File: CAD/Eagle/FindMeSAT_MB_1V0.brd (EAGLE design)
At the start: 99 x 49.2 mm, 115 parts, among them IC1111 LM2831YMF, J291 MCX-J-P-X-RA-SM1, J701 MOLEX_105017-0001, J801 MICROSIM-8P_SDCARD-8P_MOLEX-1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, J901 JST_S3B-XH-A, Q101 ABS07, U1001 CFPT-141, U101 ATXMEGA256A3BU-AU, U1011 OPA354, U1021 OPA354, U1121 LM4120IM5-3.0, U201 SIM808, U301 MPU-9250, U401 BMP180, U501 SHT31-DIS

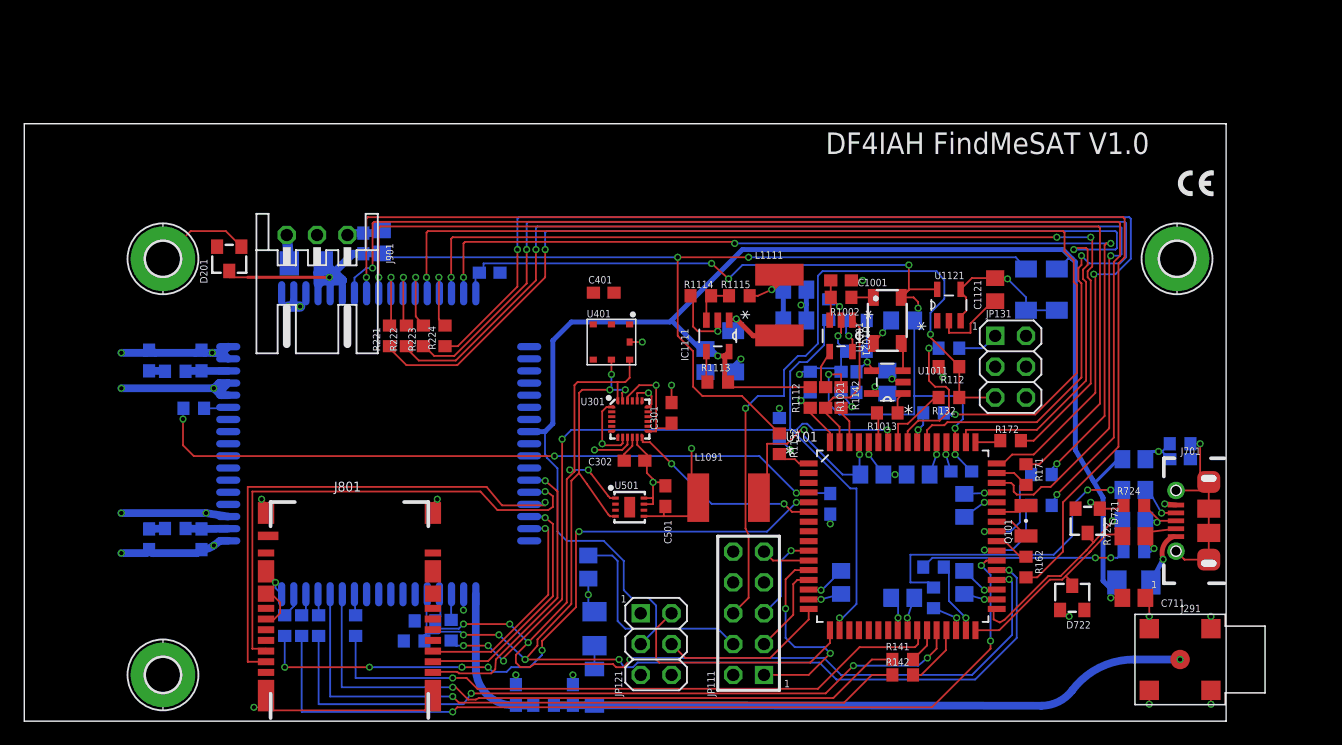
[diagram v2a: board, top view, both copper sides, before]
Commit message: Eagle - AX5243 included and library works done
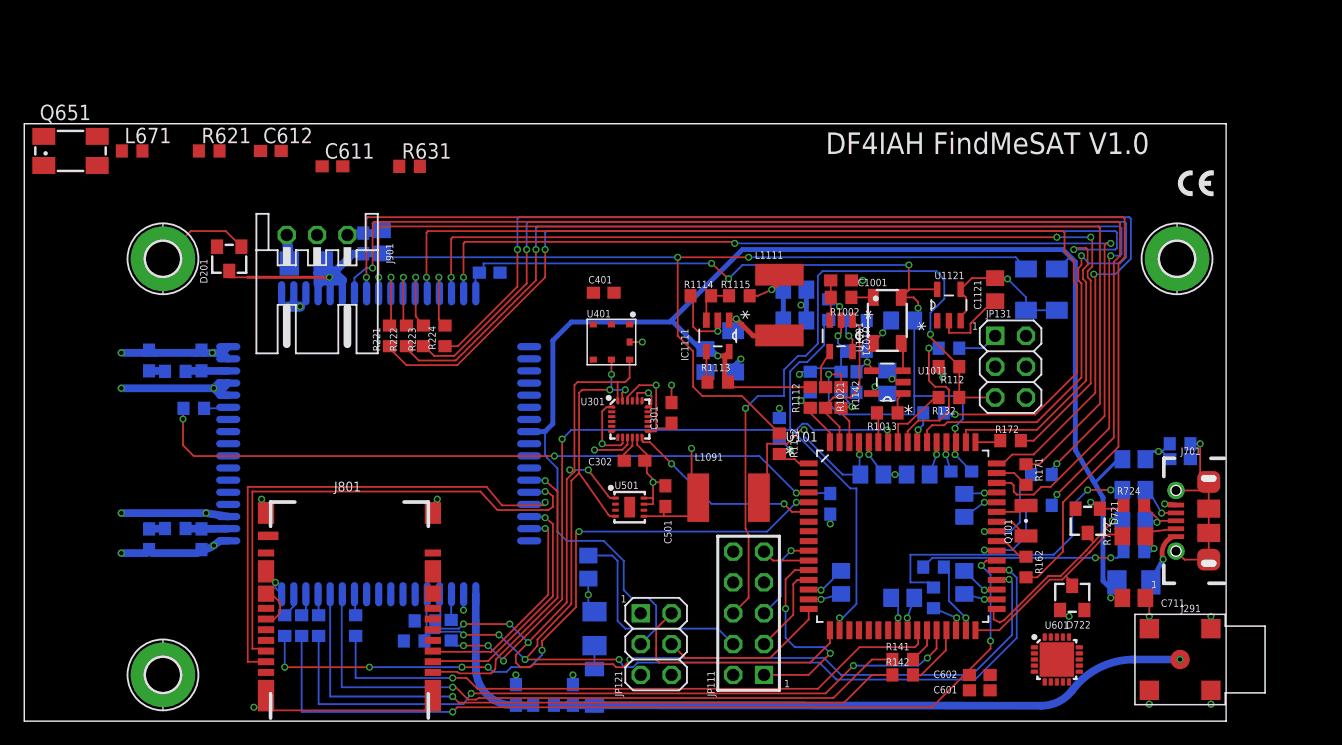
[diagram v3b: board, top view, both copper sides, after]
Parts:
- added C601: 47u, rcl:C0603
- added C602, C611, C612: 100n, rcl:C0603
- added L671: 22nH, rcl:R0603
- added Q651: ABM3B-16MHZ-10-R50-1-U, adafruit:CTS406
- added R621: 27, rcl:R0603
- added R631: 10k, rcl:R0603
- added U601: AX5243, df4iah_rf:QFN20-4X4-0P5-PAD
- U201: device df4iah_processors:SIM808 -> df4iah_gsm:SIM808
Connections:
- removed net AD_PHS_I: U101.2
- removed net AD_PHS_Q: U101.3
- removed net PULSE_I: U101.19
- removed net PULSE_Q: U101.20
- new net AX_CLK: U601.11
- new net AX_IRQ: R631.1, U601.14
- new net AX_L1: L671.1, U601.8
- new net AX_L2: L671.2, U601.7
- new net AX_MISO: R621.2, U601.12
- new net AX_MOSI: U601.13
- new net AX_SEL: U601.10
- new net CLK16N: Q651.1, U601.19
- new net CLK16P: Q651.3, U601.20
- new net N$1: C611.1, U601.1
- new net SPI_MISO: R621.1
- new net VDD_ANA@5: C612.1, U601.5
- new net VDD_IO: U601.16
- net +3V3: now also C601.1, C602.1
- net GND: now also C601.2, C602.2, C611.2, C612.2, U601.17, U601.18, U601.2, U601.21
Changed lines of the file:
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@@
 <attribute name="NAME" x="95.3008" y="8.986" size="0.6096" layer="25" ratio="20"/>
 </element>
-<element name="U201" library="df4iah_processors" package="SIM808" value="SIM808" x="29.21" y="22.86" smashed="yes" rot="MR270">
+<element name="U201" library="df4iah_gsm" package="SIM808" value="SIM808" x="29.21" y="22.86" smashed="yes" rot="MR270">
 <attribute name="NAME" x="16.002" y="35.179" size="0.8128" layer="26" ratio="20" rot="MR90"/>
 <attribute name="VALUE" x="15.24" y="34.29" size="0.4064" layer="28" ratio="10" rot="MR270"/>
@@
 <attribute name="VALUE" x="54.102" y="17.907" size="0.6096" layer="27" rot="R90"/>
 </element>
+<element name="U601" library="df4iah_rf" package="QFN20-4X4-0P5-PAD" value="AX5243" x="85.09" y="5.08"/>
+<element name="C602" library="rcl" package="C0603" value="100n" x="78.74" y="3.81" smashed="yes">
+<attribute name="NAME" x="74.93" y="3.556" size="0.6096" layer="25"/>
+<attribute name="VALUE" x="80.391" y="3.429" size="0.6096" layer="27"/>
+</element>
+<element name="C601" library="rcl" package="C0603" value="47u" x="78.74" y="2.54" smashed="yes">
+<attribute name="NAME" x="74.93" y="2.286" size="0.6096" layer="25"/>
+<attribute name="VALUE" x="80.391" y="2.286" size="0.6096" layer="27"/>
+</element>
+<element name="R621" library="rcl" package="R0603" value="27" x="15.24" y="46.99"/>
+<element name="C612" library="rcl" package="C0603" value="100n" x="20.32" y="46.99"/>
+<element name="C611" library="rcl" package="C0603" value="100n" x="25.4" y="45.72"/>
+<element name="Q651" library="adafruit" package="CTS406" value="ABM3B-16MHZ-10-R50-1-U" x="3.81" y="46.99">
+<attribute name="OC_FARNELL" value="unknown" x="3.81" y="46.99" size="0.6096" layer="27" display="off"/>
+<attribute name="MF" value="" x="3.81" y="46.99" size="0.6096" layer="27" display="off"/>
+<attribute name="OC_NEWARK" value="unknown" x="3.81" y="46.99" size="0.6096" layer="27" display="off"/>
+<attribute name="MPN" value="" x="3.81" y="46.99" size="0.6096" layer="27" display="off"/>
+</element>
+<element name="L671" library="rcl" package="R0603" value="22nH" x="8.89" y="46.99"/>
+<element name="R631" library="rcl" package="R0603" value="10k" x="31.75" y="45.72"/>
 </elements>
 <signals>
@@
 <wire x1="51.308" y1="20.447" x2="51.308" y2="21.297" width="0.15" layer="1"/>
 <wire x1="51.308" y1="21.297" x2="51.142" y2="21.463" width="0.15" layer="1"/>
+<contactref element="U601" pad="2"/>
+<contactref element="U601" pad="21"/>
+<contactref element="C602" pad="2"/>
+<contactref element="C601" pad="2"/>
+<contactref element="U601" pad="17"/>
+<contactref element="U601" pad="18"/>
+<contactref element="C611" pad="2"/>
+<contactref element="C612" pad="2"/>
 <wire x1="94.4" y1="22.86" x2="94.996" y2="38.1" width="0" layer="19" extent="16-16"/>
 <wire x1="93.98" y1="17.907" x2="94.4" y2="21.59" width="0" layer="19" extent="16-16"/>
@@
 <wire x1="92.71" y1="2.54" x2="92.71" y2="7.62" width="0" layer="19" extent="1-1"/>
 <wire x1="86.106" y1="8.636" x2="92.39" y2="10.16" width="0" layer="19" extent="1-1"/>
+<wire x1="85.59" y1="6.93" x2="86.106" y2="8.636" width="0" layer="19" extent="1-1"/>
+<wire x1="85.09" y1="6.93" x2="85.59" y2="6.93" width="0" layer="19" extent="1-1"/>
+<wire x1="85.09" y1="5.08" x2="85.09" y2="6.93" width="0" layer="19" extent="1-1"/>
+<wire x1="83.24" y1="5.58" x2="85.09" y2="5.08" width="0" layer="19" extent="1-1"/>
+<wire x1="79.59" y1="3.81" x2="83.24" y2="5.58" width="0" layer="19" extent="1-1"/>
+<wire x1="79.59" y1="2.54" x2="79.59" y2="3.81" width="0" layer="19" extent="1-1"/>
 <wire x1="80.137" y1="10.033" x2="85.36" y2="9.16" width="0" layer="19" extent="1-1"/>
 <wire x1="72.009" y1="9.591" x2="77.47" y2="10.48" width="0" layer="19" extent="16-16"/>
@@
 <wire x1="17.891" y1="39.1" x2="21.21" y2="35.26" width="0" layer="19" extent="1-16"/>
 <wire x1="26.63" y1="40.06" x2="23.21" y2="35.26" width="0" layer="19" extent="16-16"/>
+<wire x1="21.17" y1="46.99" x2="11.43" y2="3.81" width="0" layer="19" extent="1-1"/>
+<wire x1="26.25" y1="45.72" x2="21.17" y2="46.99" width="0" layer="19" extent="1-1"/>
 </signal>
 <signal name="EN">
@@
 <wire x1="52.832" y1="17.692" x2="52.705" y2="17.565" width="0.15" layer="1"/>
 <wire x1="52.705" y1="17.565" x2="52.705" y2="16.891" width="0.15" layer="1"/>
+<contactref element="C602" pad="1"/>
+<contactref element="C601" pad="1"/>
 <wire x1="75.692" y1="28.868" x2="82.55" y2="31.75" width="0" layer="19" extent="1-1"/>
 <wire x1="71.12" y1="26.99" x2="75.35" y2="29.21" width="0" layer="19" extent="1-16"/>
@@
 <wire x1="32.17" y1="8.255" x2="46.104" y2="9.02" width="0" layer="19" extent="16-16"/>
 <wire x1="31.281" y1="6.604" x2="32.17" y2="8.255" width="0" layer="19" extent="16-16"/>
+<wire x1="77.89" y1="3.81" x2="31.281" y2="6.604" width="0" layer="19" extent="1-16"/>
+<wire x1="77.89" y1="2.54" x2="77.89" y2="3.81" width="0" layer="19" extent="1-1"/>
 </signal>
 <signal name="FB">
@@
 <wire x1="75.946" y1="7.4422" x2="75.9968" y2="7.493" width="0.15" layer="1"/>
 </signal>
-<signal name="AD_PHS_I">
-<contactref element="U101" pad="2"/>
-</signal>
-<signal name="AD_PHS_Q">
-<contactref element="U101" pad="3"/>
-</signal>
 <signal name="SDA2">
 <contactref element="U101" pad="16"/>
@@
 <wire x1="52.07" y1="5.08" x2="52.07" y2="7.62" width="0.15" layer="1"/>
 <wire x1="52.07" y1="7.62" x2="53.34" y2="8.89" width="0.15" layer="1"/>
-</signal>
-<signal name="PULSE_Q">
-<contactref element="U101" pad="20"/>
-</signal>
-<signal name="PULSE_I">
-<contactref element="U101" pad="19"/>
 </signal>
 <signal name="I2C2_INT">
@@
 <wire x1="49.442" y1="22.01" x2="49.442" y2="21.463" width="0.15" layer="1"/>
 </signal>
+<signal name="VDD_IO">
+<contactref element="U601" pad="16"/>
+</signal>
+<signal name="AX_SEL">
+<contactref element="U601" pad="10"/>
+</signal>
+<signal name="AX_CLK">
+<contactref element="U601" pad="11"/>
+</signal>
+<signal name="AX_MOSI">
+<contactref element="U601" pad="13"/>
+</signal>
+<signal name="AX_MISO">
+<contactref element="U601" pad="12"/>
+<contactref element="R621" pad="2"/>
+<wire x1="16.09" y1="46.99" x2="86.94" y2="4.58" width="0" layer="19" extent="1-1"/>
+</signal>
+<signal name="SPI_MISO">
+<contactref element="R621" pad="1"/>
+</signal>
+<signal name="CLK16P">
+<contactref element="U601" pad="20"/>
+<contactref element="Q651" pad="3"/>
+<wire x1="6.01" y1="48.19" x2="84.09" y2="6.93" width="0" layer="19" extent="1-1"/>
+</signal>
+<signal name="CLK16N">
+<contactref element="U601" pad="19"/>
+<contactref element="Q651" pad="1"/>
+<wire x1="1.61" y1="45.79" x2="84.59" y2="6.93" width="0" layer="19" extent="1-1"/>
+</signal>
+<signal name="N$1">
+<contactref element="U601" pad="1"/>
+<contactref element="C611" pad="1"/>
+<wire x1="24.55" y1="45.72" x2="83.24" y2="6.08" width="0" layer="19" extent="1-1"/>
+</signal>
+<signal name="VDD_ANA@5">
+<contactref element="U601" pad="5"/>
+<contactref element="C612" pad="1"/>
+<wire x1="19.47" y1="46.99" x2="83.24" y2="4.08" width="0" layer="19" extent="1-1"/>
+</signal>
+<signal name="AX_L1">
+<contactref element="U601" pad="8"/>
+<contactref element="L671" pad="1"/>
+<wire x1="8.04" y1="46.99" x2="85.09" y2="3.23" width="0" layer="19" extent="1-1"/>
+</signal>
+<signal name="AX_L2">
+<contactref element="U601" pad="7"/>
+<contactref element="L671" pad="2"/>
+<wire x1="9.74" y1="46.99" x2="84.59" y2="3.23" width="0" layer="19" extent="1-1"/>
+</signal>
+<signal name="AX_IRQ">
+<contactref element="U601" pad="14"/>
+<contactref element="R631" pad="1"/>
+<wire x1="30.9" y1="45.72" x2="86.94" y2="5.58" width="0" layer="19" extent="1-1"/>
+</signal>
 </signals>

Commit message: Eagle - AX5243 placed and some routes are made - before SPI routing
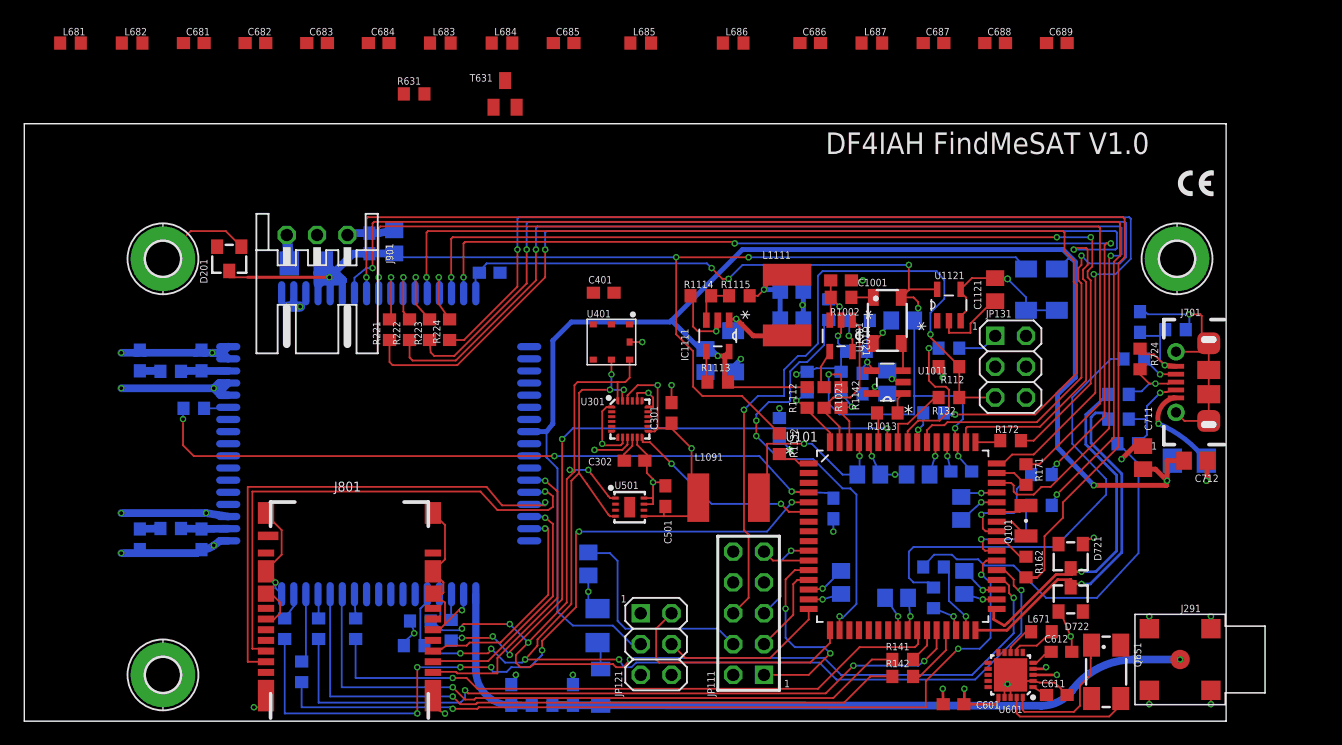
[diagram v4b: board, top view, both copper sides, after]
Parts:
- removed C602: 100n, rcl:C0603
- removed R621: 27, rcl:R0603
- added C681, C682, C683, C684: 10p, rcl:C0603
- added C685, C686: 12p, rcl:C0603
- added C687: 6.8p, rcl:C0603
- added C688, C689: 27p, rcl:C0603
- added L681, L682: 150nH, rcl:R0603
- added L683, L684: 120nH, rcl:R0603
- added L685, L686: 68nH, rcl:R0603
- added L687: 30nH, rcl:R0603
- added T631: BFS17PE6327HTSA1, df4iah_bipoltransistor:SOT23
- C601: value 47u -> 100n
- R722, R723, R725: device rcl:R0805 -> rcl:R0603
- U301: value MPU-9250 -> 9DoF IMU
- moved Q651 95.5 mm to (89.2, 4.06), turned to 270 degrees
- moved L671 84.8 mm to (83.8, 7.37)
- moved C612 77.1 mm to (85.5, 5.71)
- moved C611 73.9 mm to (85.1, 2.16)
- moved R724 12.1 mm to (91.9, 29.8), turned to 90 degrees
- moved C701 11.8 mm to (91.9, 32.9), turned to 270 degrees
- moved C711 11.6 mm to (92.2, 21.7), turned to 90 degrees
- moved J701 11.4 mm to (99.1, 27.9)
- moved RPOLY711 11.0 mm to (96.0, 21.5)
- moved R725 10.8 mm to (91.4, 29.8)
- moved R723 10.5 mm to (90.2, 26.9)
- moved R722 9.74 mm to (90.2, 24.9), flipped to the bottom, turned to 0 degrees
- moved R701 9.41 mm to (94.9, 32.3)
- moved R721 8.90 mm to (90.9, 22.9)
- moved R631 5.98 mm to (32.1, 51.7)
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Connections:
- net N$1 renamed VDD_ANA@1
- removed net SPI_MISO: R621.1
- removed net VDD_IO: U601.16
- new net AX_ANT: C687.2, C689.1, L687.2
- new net AX_ANT2: C686.2, C687.1, C688.1, L686.2, L687.1
- new net AX_ANTN: C682.1, C684.1, L682.2, U601.4
- new net AX_ANTN2: C684.2, L684.1
- new net AX_ANTN3: C686.1, L684.2, L685.2
- new net AX_ANTP: C681.2, C683.1, L681.1, U601.3
- new net AX_ANTP2: C683.2, L683.1
- new net AX_ANTP3: C685.2, L683.2, L686.1
- new net AX_IRQ_B: R631.2, T631.1
- net +3V3: now also U601.16; no longer C602.1
- net AX_CLK: now also U101.23
- net AX_IRQ: now also T631.3, U101.19
- net AX_MISO: now also U101.22; no longer R621.2
- net AX_MOSI: now also U101.21
- net AX_SEL: now also U101.20
- net CLK16N: now also Q651.3; no longer Q651.1
- net CLK16P: now also Q651.1; no longer Q651.3
- net GND: now also C681.1, C682.2, C685.1, C688.2, C689.2, L681.2, L682.1, L685.1, T631.2; no longer C602.2
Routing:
- net GND: track 168.3 -> 196.6 mm, vias 47 -> 49
- net USB_RESET: track 17.0 -> 31.0 mm, vias 2 -> 0
- net USB_D_P: track 16.2 -> 29.3 mm
- net USB_D_N: track 16.8 -> 29.7 mm, vias 0 -> 1
- net USB_ID: track 25.5 -> 37.4 mm, vias 2 -> 0
- net CLK16P: track 0.00 -> 11.4 mm
- net +3V3: track 54.3 -> 65.3 mm, vias 13 -> 15
- net CLK16N: track 0.00 -> 10.9 mm
- net GSM_NETLIGHT: track 56.0 -> 63.6 mm
- net XO_VC_PWM: track 30.5 -> 35.7 mm, vias 1 -> 3
- net GSM_STATUS_DRV: track 1.88 -> 5.69 mm
- net J_SHIELD: track 18.3 -> 22.1 mm
- net AX_L2: track 0.00 -> 3.75 mm
- net GSM_STATUS: track 73.8 -> 70.3 mm
- net VBAT: track 98.0 -> 101.3 mm
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
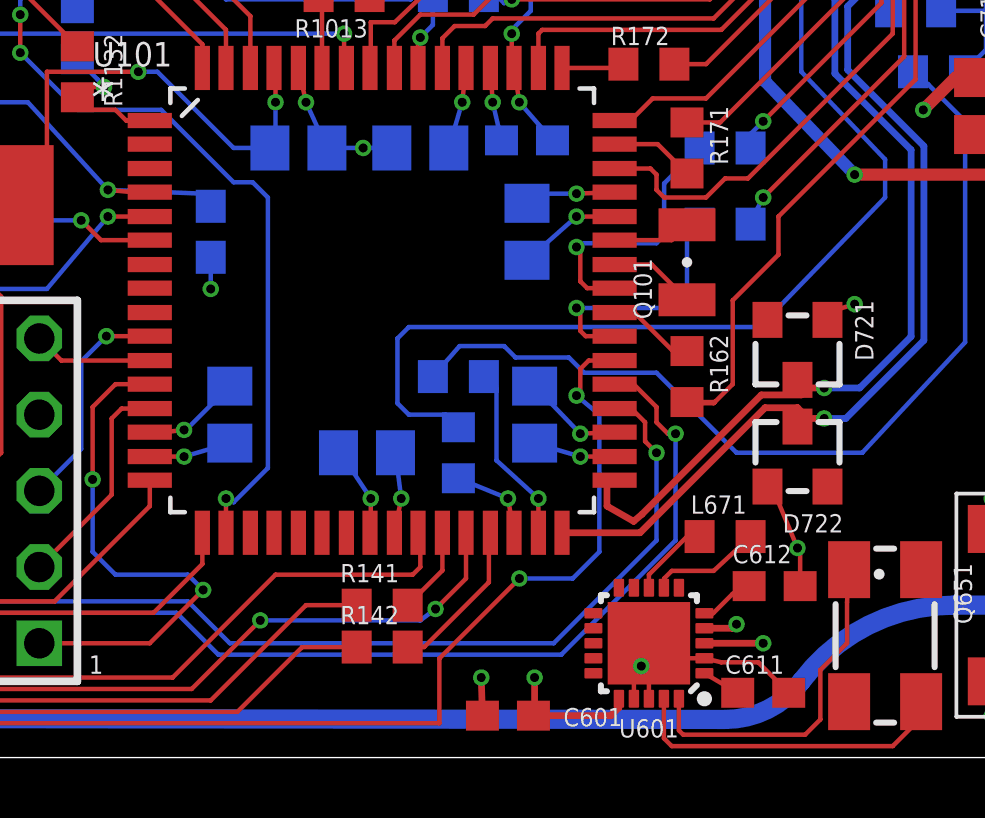
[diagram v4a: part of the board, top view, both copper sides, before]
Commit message: Eagle - AX5243 SPI routed
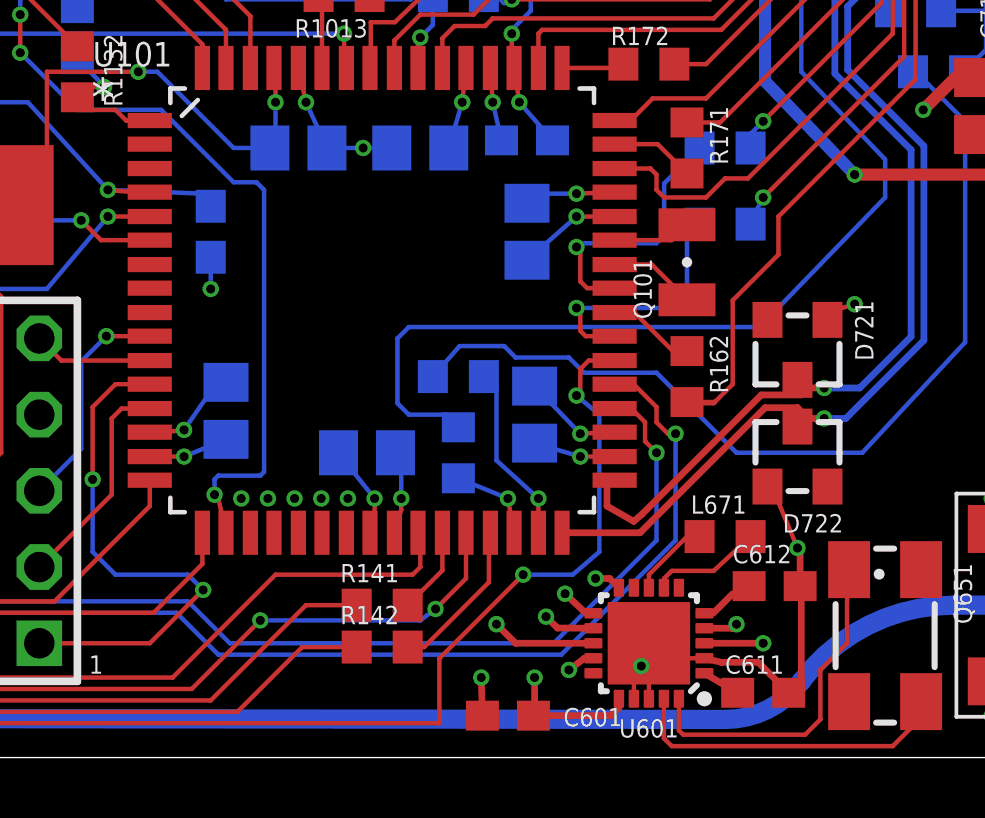
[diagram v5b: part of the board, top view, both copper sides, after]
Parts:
- moved C1091 0.18 mm to (67.2, 11.6)
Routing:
- net AX_IRQ: track 0.00 -> 14.3 mm, vias 0 -> 2
- net AX_CLK: track 0.00 -> 13.3 mm, vias 0 -> 2
- net AX_MOSI: track 0.00 -> 13.3 mm, vias 0 -> 2
- net AX_MISO: track 0.00 -> 13.3 mm, vias 0 -> 2
- net AX_SEL: track 0.00 -> 13.3 mm, vias 0 -> 2
- net GND: track 196.6 -> 200.2 mm
- net XO_VC_PWM: track 35.7 -> 36.4 mm

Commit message: Eagle - before CPU block movement one by left
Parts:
- removed C681, C682, C683, C684: 10p, rcl:C0603
- removed C687: 6.8p, rcl:C0603
- removed C688, C689: 27p, rcl:C0603
- removed L682: 150nH, rcl:R0603
- removed L683, L684: 120nH, rcl:R0603
- removed L687: 30nH, rcl:R0603
- removed R631: 10k, rcl:R0603
- removed T631: BFS17PE6327HTSA1, df4iah_bipoltransistor:SOT23
- added J681: SMA_CON, df4iah_connector:SMA_SMT_AMPHENOL_901-143
- C685: value 12p -> 22p
- C686: value 12p -> 15p
- L685, L686: value 68nH -> 82nH
- moved L681 92.4 mm to (88.0, 17.8)
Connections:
- removed net AX_ANT2: C686.2, C687.1, C688.1, L686.2, L687.1
- removed net AX_ANTN2: C684.2, L684.1
- removed net AX_ANTN3: C686.1, L684.2, L685.2
- removed net AX_ANTP2: C683.2, L683.1
- removed net AX_ANTP3: C685.2, L683.2, L686.1
- removed net AX_IRQ_B: R631.2, T631.1
- net AX_ANT: now also C686.2, J681.1, L686.2; no longer C687.2, C689.1, L687.2
- net AX_ANTN: now also C686.1, L685.2; no longer C682.1, C684.1, L682.2
- net AX_ANTP: now also C685.2, L686.1; no longer C681.2, C683.1
- net AX_IRQ: no longer R631.1, T631.3
- net GND: now also J681.2, J681.3, J681.4, J681.5; no longer C681.1, C682.2, C688.2, C689.2, L682.1, T631.2
